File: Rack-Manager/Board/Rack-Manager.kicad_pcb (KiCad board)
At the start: 2 copper layers, 36 parts, among them J1 ARJM11C7-114-BA-EW2, J2 USB4105-GT-A, U1 Ag9712-FL, U2 TPS259470A, U3 TPS259470A, U4 TLVM23625, U5 INA220, U6 STM32G0B1KCUx, U7 W6100Q

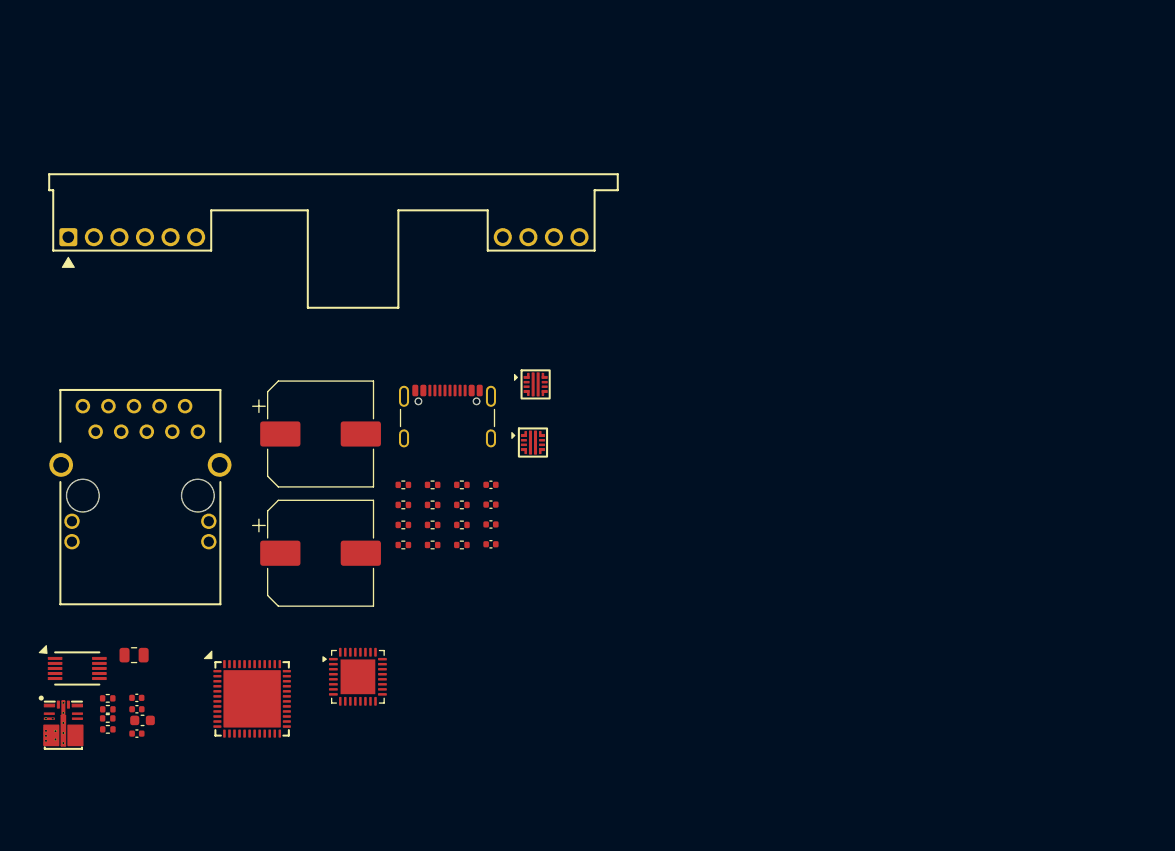
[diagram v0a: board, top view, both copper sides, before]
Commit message: Updated Texas Instruments KiCAD library. Continued with the schematics design.
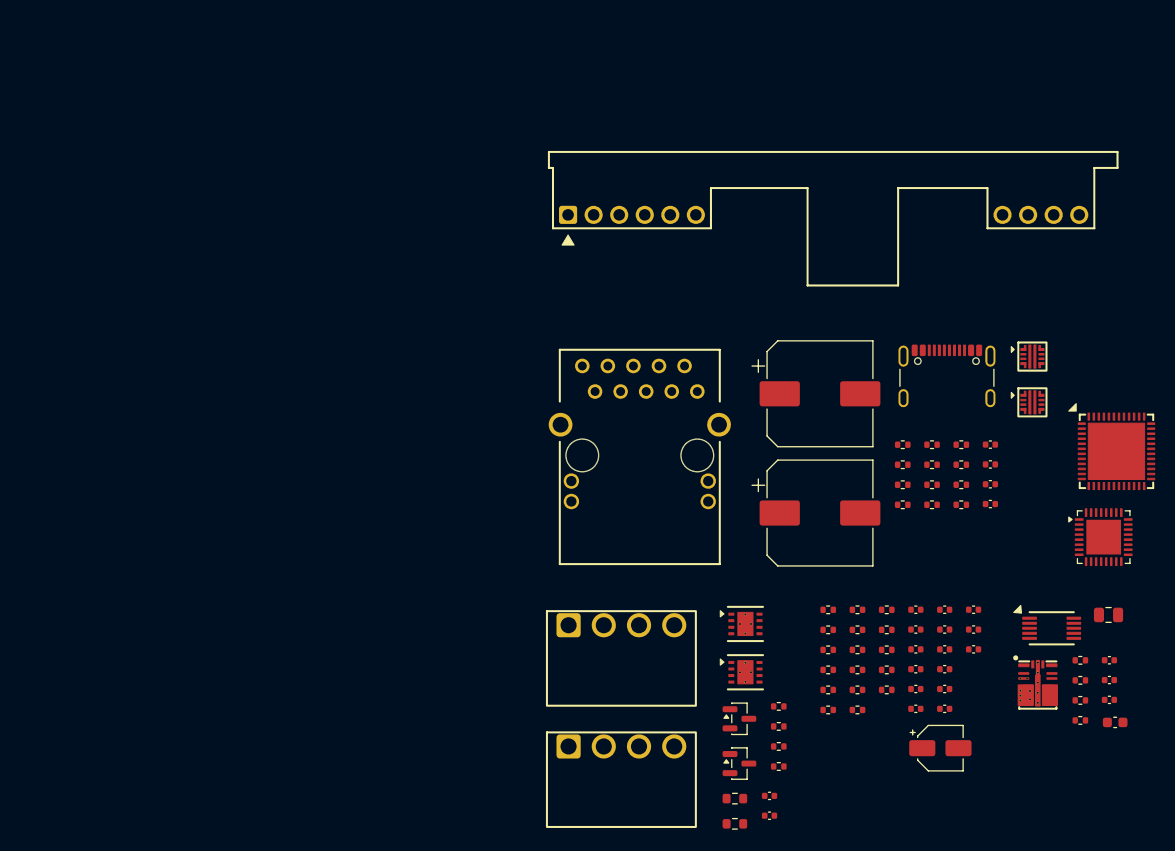
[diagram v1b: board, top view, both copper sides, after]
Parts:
- added C12: 100nF, Capacitor_SMD:C_0402_1005Metric, F.Cu at (186.6, 102.2)
- added C13: 100nF, Capacitor_SMD:C_0402_1005Metric, F.Cu at (186.6, 104.2)
- added C14: 100nF, Capacitor_SMD:C_0402_1005Metric, F.Cu at (186.6, 106.2)
- added C15: 100nF, Capacitor_SMD:C_0402_1005Metric, F.Cu at (186.6, 108.2)
- added C16: 100nF, Capacitor_SMD:C_0402_1005Metric, F.Cu at (186.6, 110.1)
- added C17: 100nF, Capacitor_SMD:C_0402_1005Metric, F.Cu at (186.6, 112.1)
- added C18: 100nF, Capacitor_SMD:C_0402_1005Metric, F.Cu at (189.4, 102.2)
- added C19: 100nF, Capacitor_SMD:C_0402_1005Metric, F.Cu at (189.4, 104.2)
- added C20: 100nF, Capacitor_SMD:C_0402_1005Metric, F.Cu at (189.4, 106.2)
- added C21: 3.3uF, Capacitor_SMD:CP_Elec_4x5.7, F.Cu at (189.0, 116.0)
- added C22: 100nF, Capacitor_SMD:C_0402_1005Metric, F.Cu at (189.4, 108.2)
- added C23: 100nF, Capacitor_SMD:C_0402_1005Metric, F.Cu at (189.4, 110.1)
- added C24: 8pF, Capacitor_SMD:C_0402_1005Metric, F.Cu at (189.4, 112.1)
- added C25: 8pF, Capacitor_SMD:C_0402_1005Metric, F.Cu at (192.3, 102.2)
- added C26: 100nF, Capacitor_SMD:C_0402_1005Metric, F.Cu at (192.3, 104.2)
- added C27: 100nF, Capacitor_SMD:C_0402_1005Metric, F.Cu at (192.3, 106.2)
- added C28: 100nF, Capacitor_SMD:C_0402_1005Metric, F.Cu at (172.0, 120.7)
- added C29: 100nF, Capacitor_SMD:C_0402_1005Metric, F.Cu at (172.0, 122.7)
- added D1: SM712, Package_TO_SOT_SMD:SOT-23, F.Cu at (169.0, 113.1)
- added D2: SM712, Package_TO_SOT_SMD:SOT-23, F.Cu at (169.0, 117.5)
- added J3: TBP03R1-350-04BE, Same Sky:TBP03R1-350-04BE, F.Cu at (152.1, 103.8)
- added J4: TBP03R1-350-04BE, Same Sky:TBP03R1-350-04BE, F.Cu at (152.1, 115.8)
- added R16: 330R, Resistor_SMD:R_0402_1005Metric, F.Cu at (177.8, 102.2)
- added R17: 330R, Resistor_SMD:R_0402_1005Metric, F.Cu at (177.8, 104.2)
- added R18: 10k, Resistor_SMD:R_0402_1005Metric, F.Cu at (177.8, 106.2)
- added R19: 10k, Resistor_SMD:R_0402_1005Metric, F.Cu at (177.8, 108.2)
- added R20: 10k, Resistor_SMD:R_0402_1005Metric, F.Cu at (177.8, 110.2)
- added R21: 10k, Resistor_SMD:R_0402_1005Metric, F.Cu at (177.8, 112.2)
- added R22: 12k, Resistor_SMD:R_0402_1005Metric, F.Cu at (180.8, 102.2)
- added R23: 300, Resistor_SMD:R_0402_1005Metric, F.Cu at (180.8, 104.2)
- added R24: 3.3, Resistor_SMD:R_0402_1005Metric, F.Cu at (180.8, 106.2)
- added R25: 3.3, Resistor_SMD:R_0402_1005Metric, F.Cu at (180.8, 108.2)
- added R26: 3.3, Resistor_SMD:R_0402_1005Metric, F.Cu at (180.8, 110.2)
- added R27: 3.3, Resistor_SMD:R_0402_1005Metric, F.Cu at (180.8, 112.2)
- added R28: 1M, Resistor_SMD:R_0402_1005Metric, F.Cu at (183.7, 102.2)
- added R29: 49.9, Resistor_SMD:R_0402_1005Metric, F.Cu at (183.7, 104.2)
- added R30: 49.9, Resistor_SMD:R_0402_1005Metric, F.Cu at (183.7, 106.2)
- added R31: 49.9, Resistor_SMD:R_0402_1005Metric, F.Cu at (183.7, 108.2)
- added R32: 49.9, Resistor_SMD:R_0402_1005Metric, F.Cu at (183.7, 110.2)
- added R33: 120, Resistor_SMD:R_0603_1608Metric, F.Cu at (168.6, 121.0)
- added R34: 10, Resistor_SMD:R_0402_1005Metric, F.Cu at (172.9, 111.8)
- added R35: 10, Resistor_SMD:R_0402_1005Metric, F.Cu at (172.9, 113.8)
- added R36: 120, Resistor_SMD:R_0603_1608Metric, F.Cu at (168.6, 123.5)
- added R37: 10, Resistor_SMD:R_0402_1005Metric, F.Cu at (172.9, 115.8)
- added R38: 10, Resistor_SMD:R_0402_1005Metric, F.Cu at (172.9, 117.8)
- added U8: THVD1450DRBR, Texas Instruments:DRB0008F, F.Cu at (169.6, 103.7)
- added U9: THVD1450DRBR, Texas Instruments:DRB0008F, F.Cu at (169.6, 108.5)
- U6: value STM32G0B1KCUx -> STM32G0B1KCU7
- moved C11 96.9 mm to (205.7, 102.8)
- moved U4 96.9 mm to (198.7, 109.7)
- moved U5 96.9 mm to (200.1, 104.1)
- moved C8 96.8 mm to (205.8, 109.2)
- moved C7 96.8 mm to (205.8, 107.3)
- moved R12 96.8 mm to (202.9, 107.3)
- moved R13 96.8 mm to (202.9, 109.3)
- moved C10 96.7 mm to (206.4, 113.4)
- moved C9 96.7 mm to (205.8, 111.2)
- moved R14 96.7 mm to (202.9, 111.2)
- moved R15 96.7 mm to (202.9, 113.2)
- moved U7 89.4 mm to (206.5, 86.5)
- moved U6 75.4 mm to (205.2, 95.0)
- moved C1 49.8 mm to (194.0, 85.8)
- moved C2 49.8 mm to (194.0, 87.8)
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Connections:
- C1 pad 2: GND -> AGND
- C10 pad 2: GND -> AGND
- C11 pad 2: GND -> AGND
- C2 pad 2: GND -> AGND
- C3 pad 2: GND -> AGND
- C4 pad 2: GND -> AGND
- C5 pad 2: GND -> AGND
- C6 pad 2: GND -> AGND
- C7 pad 2: GND -> AGND
- C8 pad 2: GND -> AGND
- C9 pad 2: GND -> AGND
- J1 pad 10: unconnected-(J1A-T_{D+}-Pad10) -> /Ethernet/TX+
- J1 pad 11: unconnected-(J1C-A_{GRN}-Pad11) -> /Ethernet/ETH_3V3D
- J1 pad 12: unconnected-(J1C-K_{GRN}-Pad12) -> Net-(J1C-K_{GRN})
- J1 pad 13: unconnected-(J1C-A_{YEL}-Pad13) -> /Ethernet/ETH_3V3D
- J1 pad 14: unconnected-(J1C-K_{YEL}-Pad14) -> Net-(J1C-K_{YEL})
- J1 pad 3: unconnected-(J1A-R_{D-}-Pad3) -> /Ethernet/RX-
- J1 pad 4: unconnected-(J1A-R_{CT}-Pad4) -> /Ethernet/ETH_3V3A
- J1 pad 5: unconnected-(J1A-R_{D+}-Pad5) -> /Ethernet/RX+
- J1 pad 8: unconnected-(J1A-T_{D-}-Pad8) -> /Ethernet/TX-
- J1 pad 9: unconnected-(J1A-T_{CT}-Pad9) -> /Ethernet/ETH_3V3A
- J2 pad A1: GND -> AGND
- J2 pad A12: GND -> AGND
- J2 pad B1: GND -> AGND
- J2 pad B12: GND -> AGND
- R10 pad 2: GND -> AGND
- R11 pad 2: GND -> AGND
- R13 pad 2: GND -> AGND
- R15 pad 2: GND -> AGND
- R4 pad 2: GND -> AGND
- R6 pad 1: GND -> AGND
- RV1 pad 1: GND -> AGND
- U1 pad 7: GND -> AGND
- U2 pad 8: GND -> AGND
- U3 pad 8: GND -> AGND
- U4 pad 10: GND -> AGND
- U7 pad 1: unconnected-(U7A-GNDA_{[1]}-Pad1) -> AGND
- U7 pad 10: unconnected-(U7A-GND_{[1]}-Pad10) -> AGND
- U7 pad 11: unconnected-(U7B-XSCO-Pad11) -> Net-(U7B-XSCO)
- U7 pad 12: unconnected-(U7B-XSCI-Pad12) -> Net-(U7B-XSCI)
- U7 pad 13: unconnected-(U7A-1V2D_{[1]}-Pad13) -> /Ethernet/ETH_1V2D
- U7 pad 14: unconnected-(U7A-1V2O-Pad14) -> /Ethernet/ETH_1V2O
- U7 pad 15: unconnected-(U7A-3V3A_{[2]}-Pad15) -> /Ethernet/ETH_3V3A
- U7 pad 16: unconnected-(U7A-GNDA_{[3]}-Pad16) -> AGND
- U7 pad 17: unconnected-(U7F-~{LINKn}-Pad17) -> /Ethernet/LED_GREEN
- U7 pad 2: unconnected-(U7E-TXO--Pad2) -> Net-(U7E-TXO-)
- U7 pad 20: unconnected-(U7F-~{ACTIVEn}-Pad20) -> /Ethernet/LED_YELLOW
- U7 pad 22: unconnected-(U7A-1V2D_{[2]}-Pad22) -> /Ethernet/ETH_1V2D
- U7 pad 24: unconnected-(U7A-3V3D_{[1]}-Pad24) -> /Ethernet/ETH_3V3D
- U7 pad 25: unconnected-(U7B-MODE_{[0]}-Pad25) -> Net-(U7B-MODE_{[0]})
- U7 pad 26: unconnected-(U7B-MODE_{[1]}-Pad26) -> Net-(U7B-MODE_{[1]})
- U7 pad 27: unconnected-(U7B-MODE_{[2]}-Pad27) -> Net-(U7B-MODE_{[2]})
- U7 pad 28: unconnected-(U7B-MODE_{[3]}-Pad28) -> Net-(U7B-MODE_{[3]})
- U7 pad 29: unconnected-(U7C-~{CSn}-Pad29) -> /MCU/ETH_CS
- U7 pad 3: unconnected-(U7E-TXO+-Pad3) -> Net-(U7E-TXO+)
- U7 pad 30: unconnected-(U7C-SCLK-Pad30) -> /MCU/ETH_SCLK
- U7 pad 31: unconnected-(U7A-1V2D_{[3]}-Pad31) -> /Ethernet/ETH_1V2D
- U7 pad 32: unconnected-(U7C-MOSI-Pad32) -> /MCU/ETH_MOSI
- U7 pad 33: unconnected-(U7C-MISO-Pad33) -> /MCU/ETH_MISO
- U7 pad 36: unconnected-(U7A-3V3D_{[2]}-Pad36) -> /Ethernet/ETH_3V3D
- U7 pad 4: unconnected-(U7A-1V2A-Pad4) -> /Ethernet/ETH_1V2A
- U7 pad 45: unconnected-(U7A-1V2D_{[4]}-Pad45) -> /Ethernet/ETH_1V2D
- U7 pad 46: unconnected-(U7A-GND_{[2]}-Pad46) -> AGND
- U7 pad 47: unconnected-(U7B-~{INTn}-Pad47) -> /MCU/~{ETH_INT}
- U7 pad 48: unconnected-(U7B-~{RSTn}-Pad48) -> /MCU/~{ETH_RST}
- U7 pad 49: unconnected-(U7A-THERMAL_PAD-Pad49) -> AGND
- U7 pad 5: unconnected-(U7E-RXI--Pad5) -> Net-(U7E-RXI-)
- U7 pad 6: unconnected-(U7E-RXI+-Pad6) -> Net-(U7E-RXI+)
- U7 pad 7: unconnected-(U7A-GNDA_{[2]}-Pad7) -> AGND
- U7 pad 8: unconnected-(U7A-3V3A_{[1]}-Pad8) -> /Ethernet/ETH_3V3A
- U7 pad 9: unconnected-(U7B-RSET_BG-Pad9) -> Net-(U7B-RSET_BG)

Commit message: Added Bourns library, updated Texas Instruments library, continued with schematic drawing.
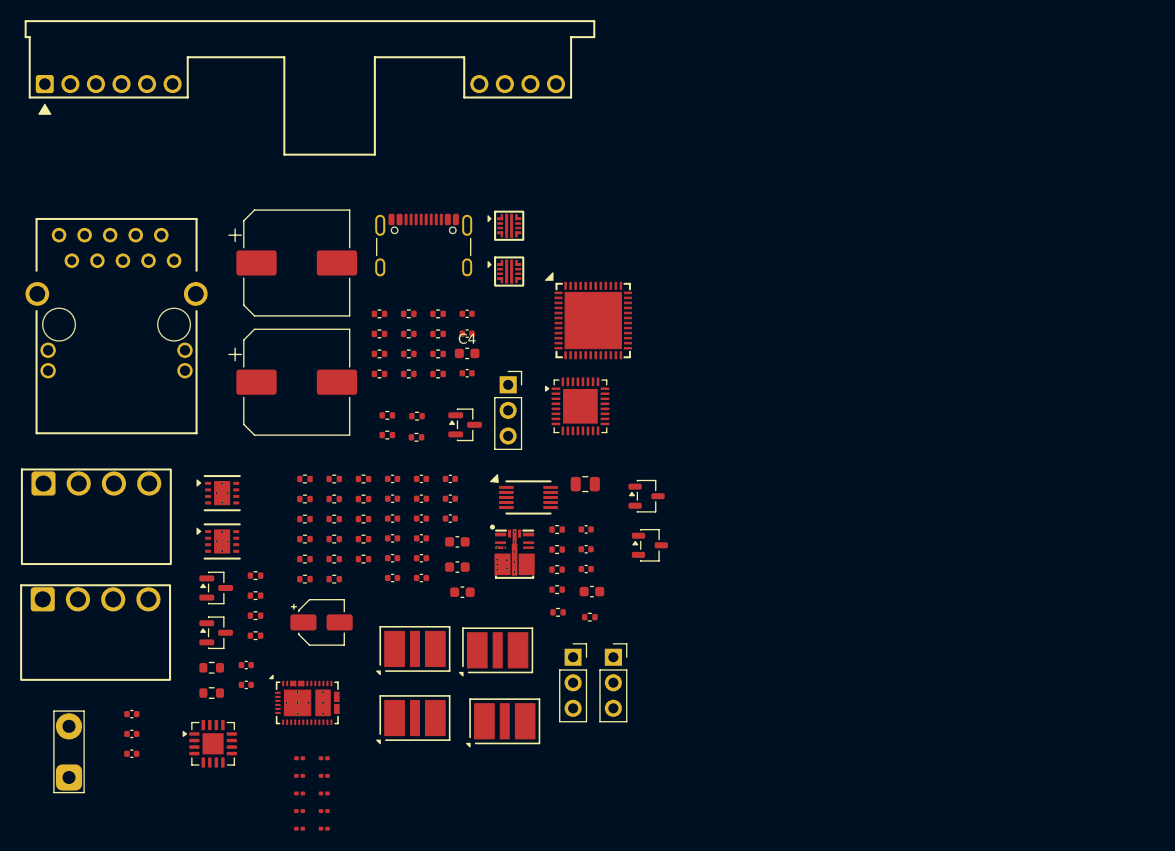
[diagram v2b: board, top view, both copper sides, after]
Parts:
- added C3: ~, Capacitor_SMD:C_0603_1608Metric, F.Cu at (141.0, 95.5)
- added C32: 100nF, Capacitor_SMD:C_0402_1005Metric, F.Cu at (108.6, 112.6)
- added C33: 100nF, Capacitor_SMD:C_0402_1005Metric, F.Cu at (108.6, 114.6)
- added C34: 100nF, Capacitor_SMD:C_0402_1005Metric, F.Cu at (108.6, 116.6)
- added C5: ~, Capacitor_SMD:C_0603_1608Metric, F.Cu at (141.0, 98.0)
- added C6: ~, Capacitor_SMD:C_0603_1608Metric, F.Cu at (141.5, 100.5)
- added D2: SM712, Package_TO_SOT_SMD:SOT-23, F.Cu at (141.8, 83.9)
- added F1: TBU-CA065-300-WH, Bourns:TBU-CA, F.Cu at (136.8, 106.1)
- added F2: TBU-CA065-300-WH, Bourns:TBU-CA, F.Cu at (145.0, 106.3)
- added F3: TBU-CA065-300-WH, Bourns:TBU-CA, F.Cu at (136.8, 113.0)
- added F4: TBU-CA065-300-WH, Bourns:TBU-CA, F.Cu at (145.7, 113.3)
- added J5: Conn_01x03_Pin, Connector_PinSocket_2.54mm:PinSocket_1x03_P2.54mm_Vertical, F.Cu at (146.0, 79.9)
- added J5: Conn_01x03_Pin, Connector_PinSocket_2.54mm:PinSocket_1x03_P2.54mm_Vertical, F.Cu at (152.5, 107.0)
- added J6: Conn_01x03_Pin, Connector_PinSocket_2.54mm:PinSocket_1x03_P2.54mm_Vertical, F.Cu at (156.5, 107.0)
- added JP1: Jumper_3_Bridged12, TestPoint:TestPoint_2Pads_Pitch5.08mm_Drill1.3mm, F.Cu at (102.4, 118.9)
- added Q1: NTR4003NT1G, Package_TO_SOT_SMD:SOT-23-3, F.Cu at (160.1, 95.8)
- added Q3: NTR4003NT1G, Package_TO_SOT_SMD:SOT-23-3, F.Cu at (159.8, 91.0)
- added R33: 120, Resistor_SMD:R_0402_1005Metric, F.Cu at (151.0, 102.5)
- added R39: 10k, Resistor_SMD:R_0402_1005Metric, F.Cu at (134.0, 82.9)
- added R40: 10k, Resistor_SMD:R_0402_1005Metric, F.Cu at (137.0, 83.0)
- added R41: 10k, Resistor_SMD:R_0402_1005Metric, F.Cu at (134.0, 84.9)
- added R42: 10k, Resistor_SMD:R_0402_1005Metric, F.Cu at (136.9, 85.1)
- added R43: 10k, Resistor_SMD:R_0201_0603Metric, F.Cu at (125.3, 117.0)
- added R44: 10k, Resistor_SMD:R_0201_0603Metric, F.Cu at (125.3, 118.8)
- added R45: 10k, Resistor_SMD:R_0201_0603Metric, F.Cu at (125.3, 120.5)
- added R46: 10k, Resistor_SMD:R_0201_0603Metric, F.Cu at (125.3, 122.2)
- added R48: 10k, Resistor_SMD:R_0201_0603Metric, F.Cu at (125.3, 124.0)
- added R55: 10k, Resistor_SMD:R_0201_0603Metric, F.Cu at (127.8, 117.0)
- added R56: 10k, Resistor_SMD:R_0201_0603Metric, F.Cu at (127.8, 118.8)
- added R57: 10k, Resistor_SMD:R_0201_0603Metric, F.Cu at (127.8, 120.5)
- added R58: 10k, Resistor_SMD:R_0201_0603Metric, F.Cu at (127.8, 122.2)
- added R59: 10k, Resistor_SMD:R_0402_1005Metric, F.Cu at (154.2, 103.0)
- added R60: 10k, Resistor_SMD:R_0201_0603Metric, F.Cu at (127.8, 124.0)
- added U10: INA3221, Package_DFN_QFN:Texas_RGV0016A_VQFN-16-1EP_4x4mm_P0.65mm_EP2.1x2.1mm, F.Cu at (116.7, 115.6)
- added U11: TPS25730D, Texas Instruments:REF0038A, F.Cu at (126.1, 111.5)
- C4: renamed from C3; footprint Capacitor_SMD:C_0402_1005Metric -> Capacitor_SMD:C_0603_1608Metric
- moved C18 62.8 mm to (127.5, 103.5)
- moved J4 54.3 mm to (99.8, 101.2)
- moved J3 54.0 mm to (99.9, 89.7)
- moved C30 53.6 mm to (120.0, 109.7)
- moved C31 53.6 mm to (120.0, 107.7)
- moved R33 53.6 mm to (116.6, 108.0)
- moved R36 53.6 mm to (116.6, 110.5)
- moved C1 53.6 mm to (142.0, 72.8)
- moved C10 53.6 mm to (154.4, 100.4)
- moved C11 53.6 mm to (153.8, 94.3)
- moved C12 53.6 mm to (153.8, 96.2)
- moved C13 53.6 mm to (153.8, 98.2)
- moved C14 53.6 mm to (134.6, 99.1)
- moved C15 53.6 mm to (137.4, 89.2)
- moved C16 53.6 mm to (137.4, 91.2)
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- renumbered C7 to C11, C8 to C12, C9 to C13, C17 to C14, C18 to C15, C19 to C16, C20 to C17, C21 to C18, C12 to C19, C13 to C20, C14 to C21, C15 to C22, C16 to C23, C26 to C24, C27 to C25, C22 to C26, C23 to C27, C24 to C28, C25 to C29, C29 to C30, C28 to C31, C5 to C7, C6 to C8, C11 to C9
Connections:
- net /RS-485/V_{BUS}1 renamed /Bus output/V_{BUS}1
- net /RS-485/V_{BUS}2 renamed /Bus output/V_{BUS}2
- D1 pad 1: /RS-485/A2 -> Net-(D1-A1)
- D1 pad 2: /RS-485/B2 -> Net-(D1-A2)
- D2 pad 1: /RS-485/A2 -> Net-(D2-A1)
- D2 pad 2: /RS-485/B2 -> Net-(D2-A2)
- J3 pad 3: /RS-485/A1 -> A1
- J3 pad 4: /RS-485/B1 -> B1
- J4 pad 3: /RS-485/A2 -> A2
- J4 pad 4: /RS-485/B2 -> B2
- R34 pad 1: Net-(U8-A) -> Net-(J5-Pin_1)
- R34 pad 2: /RS-485/A2 -> Net-(D1-A1)
- R35 pad 2: /RS-485/B2 -> Net-(D1-A2)
- R36 pad 1: Net-(U9-A) -> Net-(J6-Pin_3)
- R37 pad 1: Net-(U9-A) -> Net-(J6-Pin_1)
- R37 pad 2: /RS-485/A2 -> Net-(D2-A1)
- R38 pad 2: /RS-485/B2 -> Net-(D2-A2)
- U8 pad 6: Net-(U8-A) -> Net-(J5-Pin_1)
- U9 pad 6: Net-(U9-A) -> Net-(J6-Pin_1)
